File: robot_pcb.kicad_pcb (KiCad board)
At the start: 2 copper layers, 140 x 180 mm, 190 parts, among them J1 Raspberry_Pi_2_3, J10 Servo_TrayRelease, J11 BATT BYPASS, J12 12V BYPASS, J14 Motor FR, J17 Conn_01x04, J18 USB_C_Receptacle_PowerOnly_6P, J19 3V3 BYPASS, J20 5V BYPASS, J21 5.1V BYPASS, J23 Motor BR, J25 ConductClaw, J26 Motor BL, J27 TOF_Front, J28 OLED_Display, J29 Motor FL, J3 Lipo, J6 TOF_Claw, J7 UltraS_Side, J8 Servo_Grab, J9 Servo_Lift, Q2 Q_NMOS_GDS, SW1 SW_SPDT, SW2 SW_Push, U1 STM32F407VGTx, U10 DMG2305UX-7, U11 DMG2305UX-7, U2 BQ76920PW, U3 AP64501SP-13, U4 MAX25240AFFD/VY+, U5 DMG2305UX-7, U6 AP64501SP-13, U7 AP64501SP-13, U9 BNO086, Y1 25MHz, Y2 32.768kHz

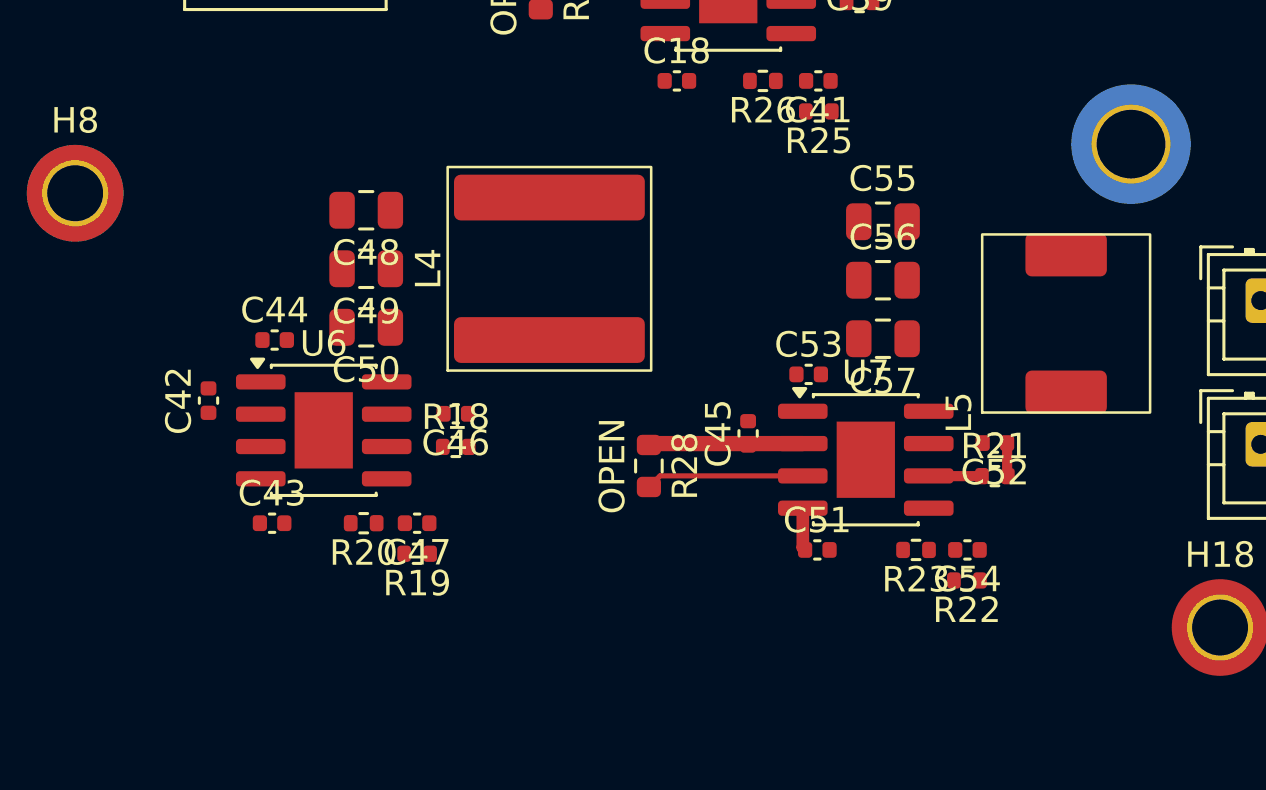
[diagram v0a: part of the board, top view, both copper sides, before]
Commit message: routing voltage reguulators
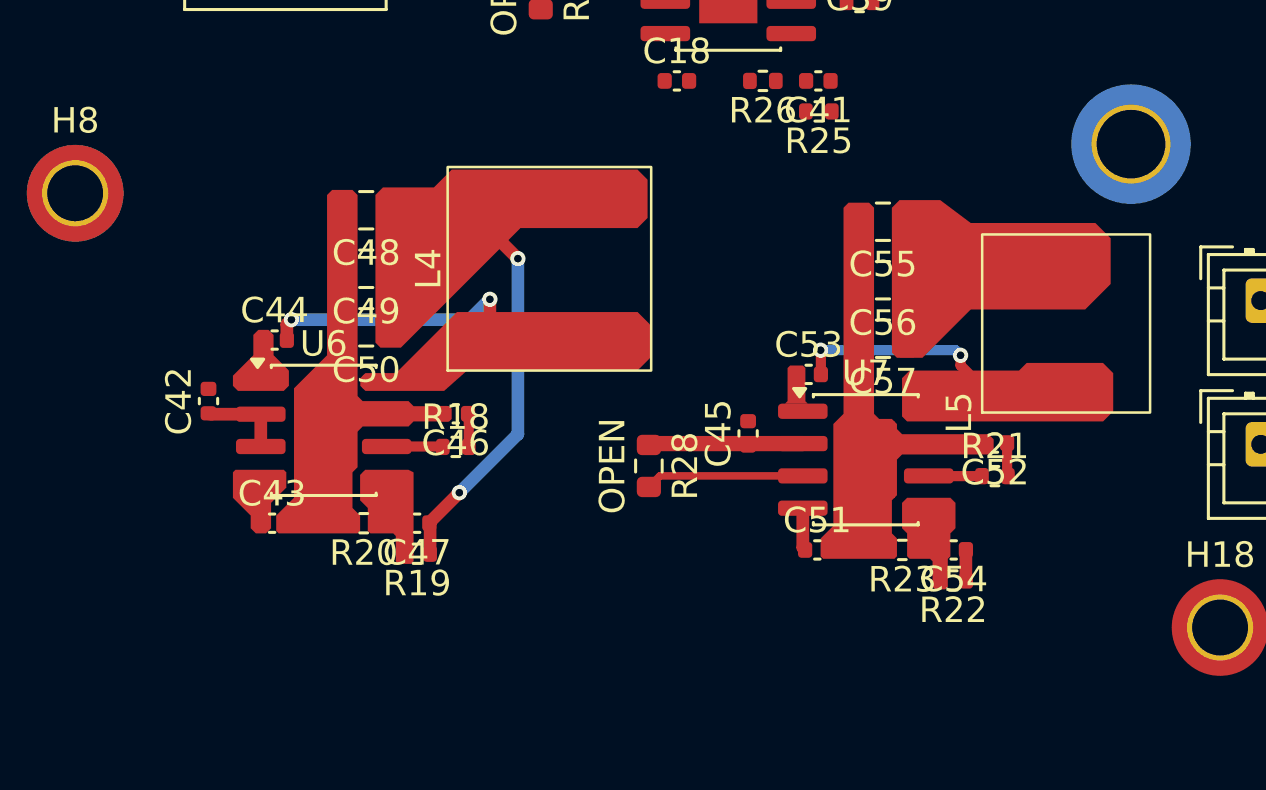
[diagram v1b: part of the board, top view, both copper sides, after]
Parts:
- moved C54 0.54 mm to (148.4, 180.7)
- moved R22 0.54 mm to (148.4, 181.8)
- moved R23 0.54 mm to (146.4, 180.7)
- turned C55 to 180 degrees
- turned C56 to 180 degrees
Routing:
- net /Regulators/5.1V: track 0.00 -> 14.1 mm, vias 0 -> 2
- net Net-(U6-SW): track 0.00 -> 11.3 mm, vias 0 -> 2
- net Net-(U7-SW): track 0.00 -> 9.22 mm, vias 0 -> 2
- net /Regulators/SUP: track 6.07 -> 9.42 mm
- net Net-(U6-COMP): track 0.00 -> 2.21 mm
- net Net-(C46-Pad1): track 0.00 -> 1.31 mm
- net /Regulators/3.3V: track 0.00 -> 1.20 mm

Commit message: updated pcb
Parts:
- removed J11: BATT BYPASS, Connector_JST:JST_XH_B2B-XH-A_1x02_P2.50mm_Vertical
- removed J12: 12V BYPASS, Connector_JST:JST_XH_B2B-XH-A_1x02_P2.50mm_Vertical
- removed J19: 3V3 BYPASS, Connector_JST:JST_XH_B2B-XH-A_1x02_P2.50mm_Vertical
- removed J20: 5V BYPASS, Connector_JST:JST_XH_B2B-XH-A_1x02_P2.50mm_Vertical
- removed J21: 5.1V BYPASS, Connector_JST:JST_XH_B2B-XH-A_1x02_P2.50mm_Vertical
- added J2: Power_Bypass, Connector_PinHeader_2.54mm:PinHeader_1x06_P2.54mm_Vertical, F.Cu at (170.5, 80.5)
- SW1: footprint Button_Switch_THT:SW_TH_Tactile_Omron_B3F-112x -> Button_Switch_THT:SW_Slide-03_Wuerth-WS-SLTV_10x2.5x6.4_P2.54mm

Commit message: wired up some motor drivers, idk if this is right tho
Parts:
- C74, C75, C76, C77, R36, R37, U15, U16: moved to B.Cu
- moved R36 28.2 mm to (118.3, 59.7), turned to -90 degrees
- moved U15 23.7 mm to (115.5, 58.2), turned to 90 degrees
- moved C75 19.5 mm to (116.4, 62.2), turned to -90 degrees
- moved C74 18.7 mm to (114.9, 55.2), turned to 180 degrees
- moved C77 14.9 mm to (89.2, 46.3)
- moved R37 7.30 mm to (87.3, 48.8), turned to 90 degrees
- moved C76 5.11 mm to (90.8, 53.2), turned to 0 degrees
- moved U16 0.12 mm to (90.2, 50.2)
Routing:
- net Net-(U15-SNS): track 0.00 -> 10.9 mm, vias 0 -> 2
- net +12V: track 13.8 -> 20.8 mm
- net Net-(U16-SNS): track 4.12 -> 10.8 mm, vias 0 -> 2
- net /BL_M2: track 0.00 -> 6.46 mm
- net /BL_M1: track 0.00 -> 6.45 mm
- net /BR_M1: track 9.28 -> 6.50 mm
- net /BR_M2: track 9.28 -> 6.55 mm

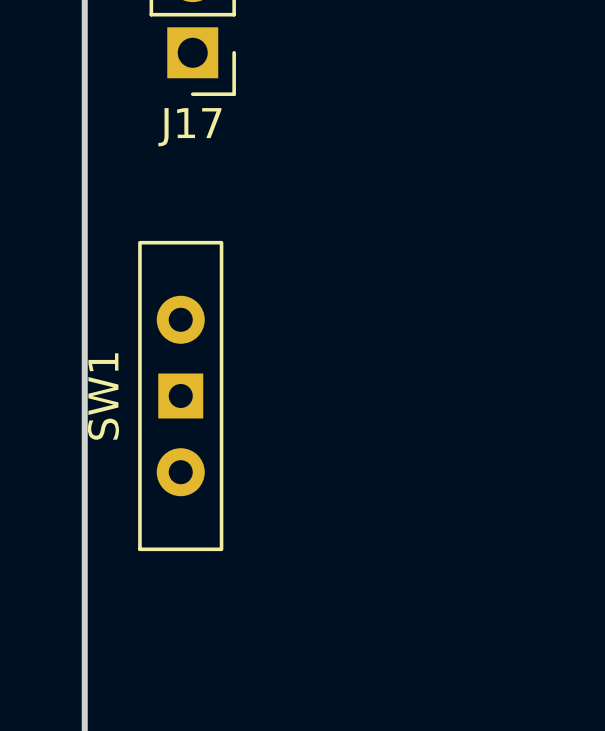
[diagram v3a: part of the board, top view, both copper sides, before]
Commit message: changed switch footprint for stm32 boot0
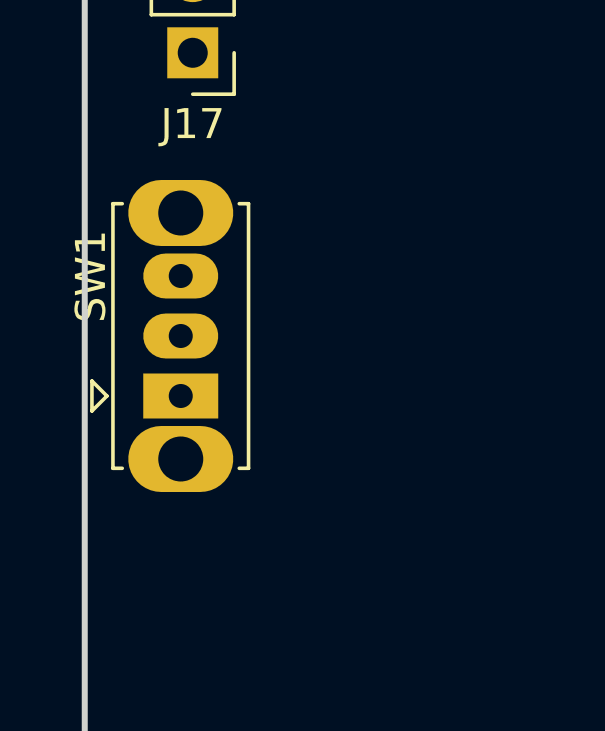
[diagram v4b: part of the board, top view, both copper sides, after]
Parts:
- SW1: footprint Button_Switch_THT:SW_Slide-03_Wuerth-WS-SLTV_10x2.5x6.4_P2.54mm -> Button_Switch_THT:SW_Slide_SPDT_Straight_CK_OS102011MS2Q

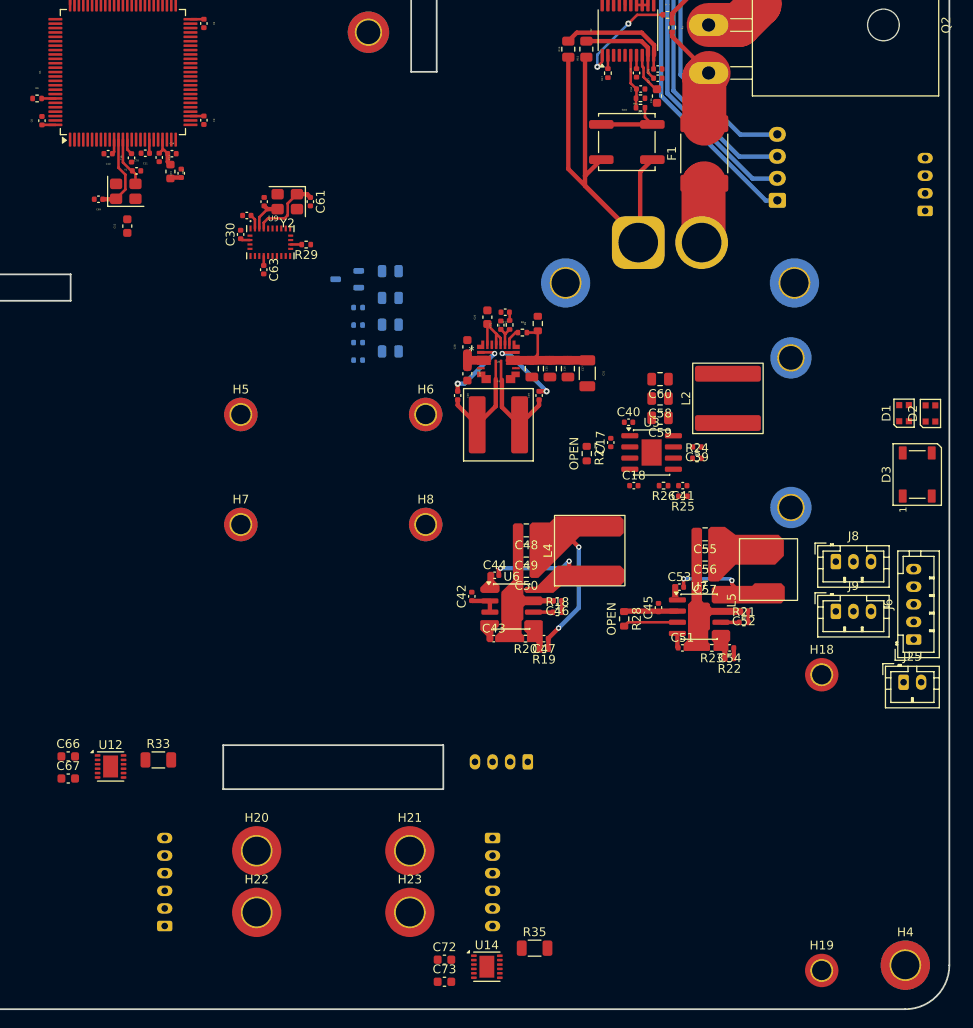
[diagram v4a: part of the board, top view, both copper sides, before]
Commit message: finished wiring motor drivers and moved boot button
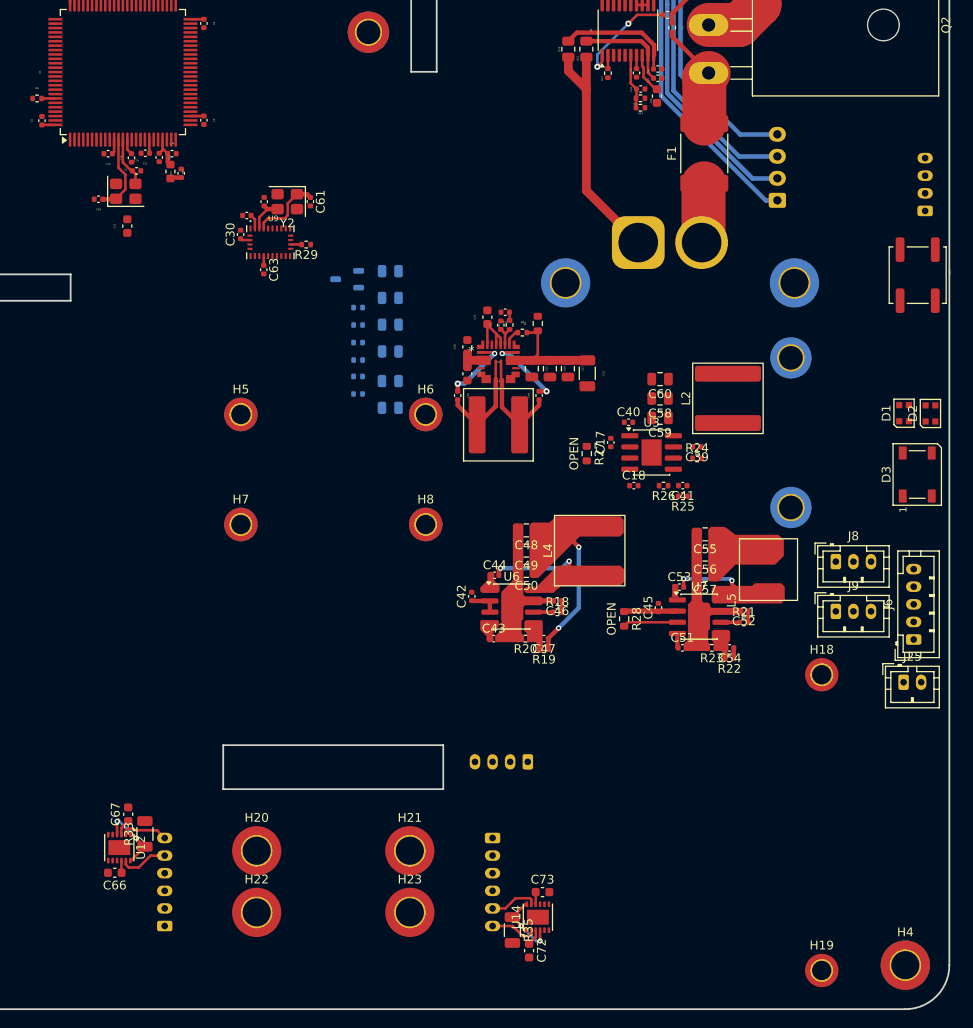
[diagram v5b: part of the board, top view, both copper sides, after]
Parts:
- added D8: LED, LED_SMD:LED_0805_2012Metric, B.Cu at (109.9, 150.3)
- added D9: LED, LED_SMD:LED_0805_2012Metric, B.Cu at (109.9, 153.4)
- added R40: 250, Resistor_SMD:R_0402_1005Metric, B.Cu at (106.2, 149.8)
- added R41: 250, Resistor_SMD:R_0402_1005Metric, B.Cu at (106.2, 151.8)
- moved SW2 36.3 mm to (169.8, 138.3), turned to 90 degrees
- moved C73 15.1 mm to (127.2, 208.4)
- moved C66 14.2 mm to (78.6, 206.2), turned to 180 degrees
- moved C72 9.67 mm to (125.7, 215.1), turned to -90 degrees
- moved U12 9.27 mm to (79.1, 203.3), turned to -90 degrees
- moved R33 8.54 mm to (82.0, 201.8), turned to 90 degrees
- moved U14 8.08 mm to (126.7, 211.2), turned to 90 degrees
- moved C67 7.93 mm to (80.1, 199.6), turned to 90 degrees
- moved R35 3.25 mm to (123.8, 212.7), turned to -90 degrees
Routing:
- net +BATT: track 63.9 -> 31.9 mm
- net Net-(U12-SNS): track 0.00 -> 9.03 mm, vias 0 -> 2
- net Net-(U14-SNS): track 0.00 -> 8.64 mm, vias 0 -> 2
- net /Battery/TS1_SW: track 8.05 -> 0.00 mm
- net +12V: track 20.8 -> 27.3 mm
- net /FR_M2: track 0.00 -> 5.57 mm
- net /FL_M2: track 0.00 -> 5.46 mm
- net /FL_M1: track 0.00 -> 5.41 mm
- net /FR_M1: track 0.00 -> 5.38 mm

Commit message: attempted to wire some stuff, its a bit of a mess tho feel free to delete
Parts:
- moved C12 7.50 mm to (77.2, 125.8), turned to 180 degrees
- moved R6 0.87 mm to (70.3, 118.9), turned to 90 degrees
- moved J27 0.70 mm to (126.2, 193.6)
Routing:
- net /I2C_SCL: track 0.00 -> 196.5 mm, vias 0 -> 5
- net /I2C_SDA: track 0.00 -> 195.7 mm, vias 0 -> 4
- net /TIM1_CH1: track 0.00 -> 109.8 mm, vias 0 -> 1
- net /TIM1_CH2: track 0.00 -> 108.8 mm, vias 0 -> 1
- net /PD9: track 0.00 -> 108.5 mm, vias 0 -> 2
- net /TIM2_CH1: track 0.00 -> 106.6 mm, vias 0 -> 1
- net /TIM2_CH2: track 0.00 -> 104.7 mm, vias 0 -> 1
- net /TIM5_CH2: track 0.00 -> 87.9 mm, vias 0 -> 2
- net /TIM3_CH2: track 0.00 -> 85.2 mm
- net /TIM3_CH1: track 0.00 -> 84.2 mm
- net /TIM5_CH4: track 0.00 -> 83.9 mm, vias 0 -> 1
- net /PD11: track 0.00 -> 63.9 mm, vias 0 -> 1
- net /TIM4_CH1: track 0.00 -> 59.7 mm, vias 0 -> 1
- net /TIM4_CH2: track 0.00 -> 57.1 mm, vias 0 -> 1
- net +3.3V: track 13.4 -> 14.8 mm

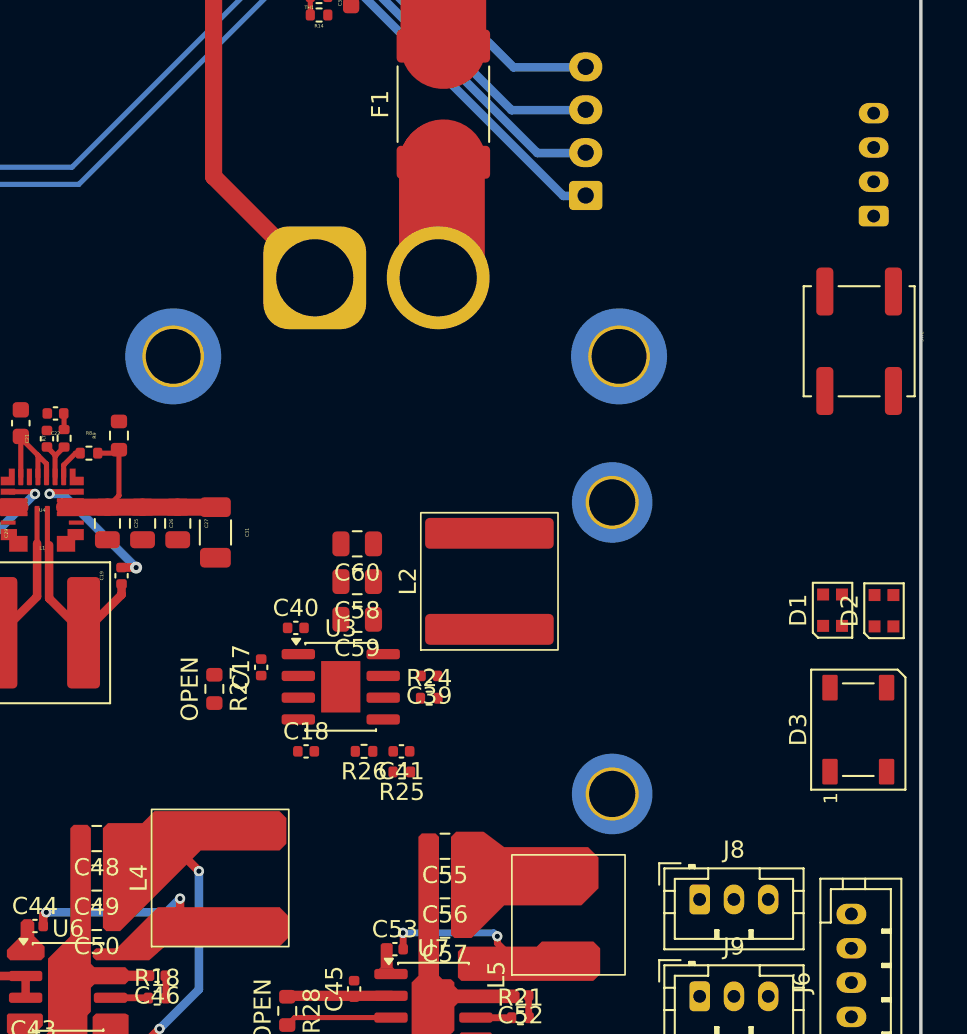
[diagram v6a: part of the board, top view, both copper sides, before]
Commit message: route last regulator and changed ultrasonic connector
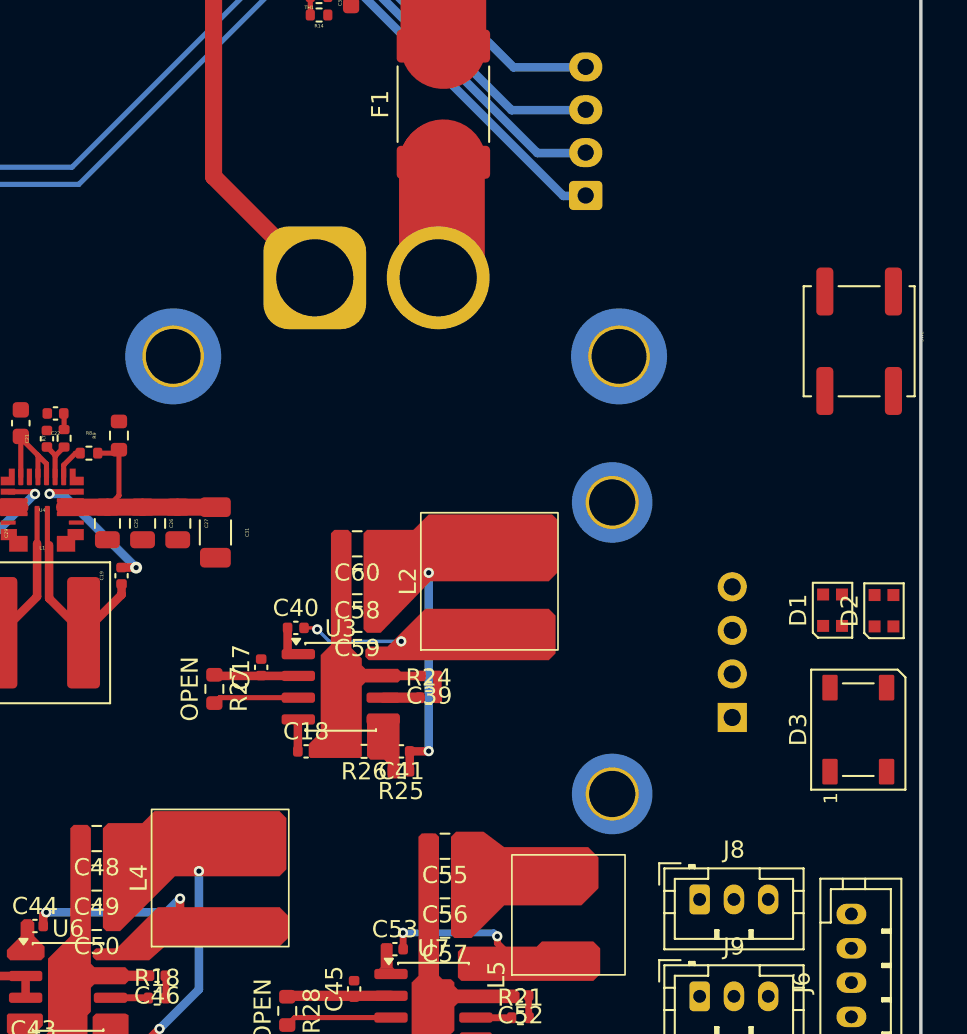
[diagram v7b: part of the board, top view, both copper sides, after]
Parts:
- J7: footprint Connector_JST:JST_PH_B4B-PH-K_1x04_P2.00mm_Vertical -> Connector_PinHeader_2.54mm:PinHeader_1x04_P2.54mm_Vertical
- moved J7 30.4 mm to (162.4, 160.2), turned to 0 degrees
- moved R25 0.07 mm to (143.1, 163.4)
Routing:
- net /Regulators/5V: track 0.00 -> 12.7 mm, vias 0 -> 2
- net Net-(U3-SW): track 0.00 -> 6.00 mm, vias 0 -> 2
- net /Regulators/5VEN: track 0.00 -> 5.03 mm
- net /Regulators/SUP: track 9.42 -> 14.3 mm
- net GND: track 2.54 -> 4.74 mm
- net Net-(U3-BST): track 0.00 -> 2.16 mm
- net Net-(U3-COMP): track 0.00 -> 2.15 mm
- net Net-(U3-SS): track 0.00 -> 1.87 mm
- net Net-(C39-Pad1): track 0.00 -> 1.31 mm
